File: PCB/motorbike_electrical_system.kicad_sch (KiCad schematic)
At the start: 8 parts, among them U1 L7805, U2 L7805, U3 L7805, U4 ATmega16L-8P

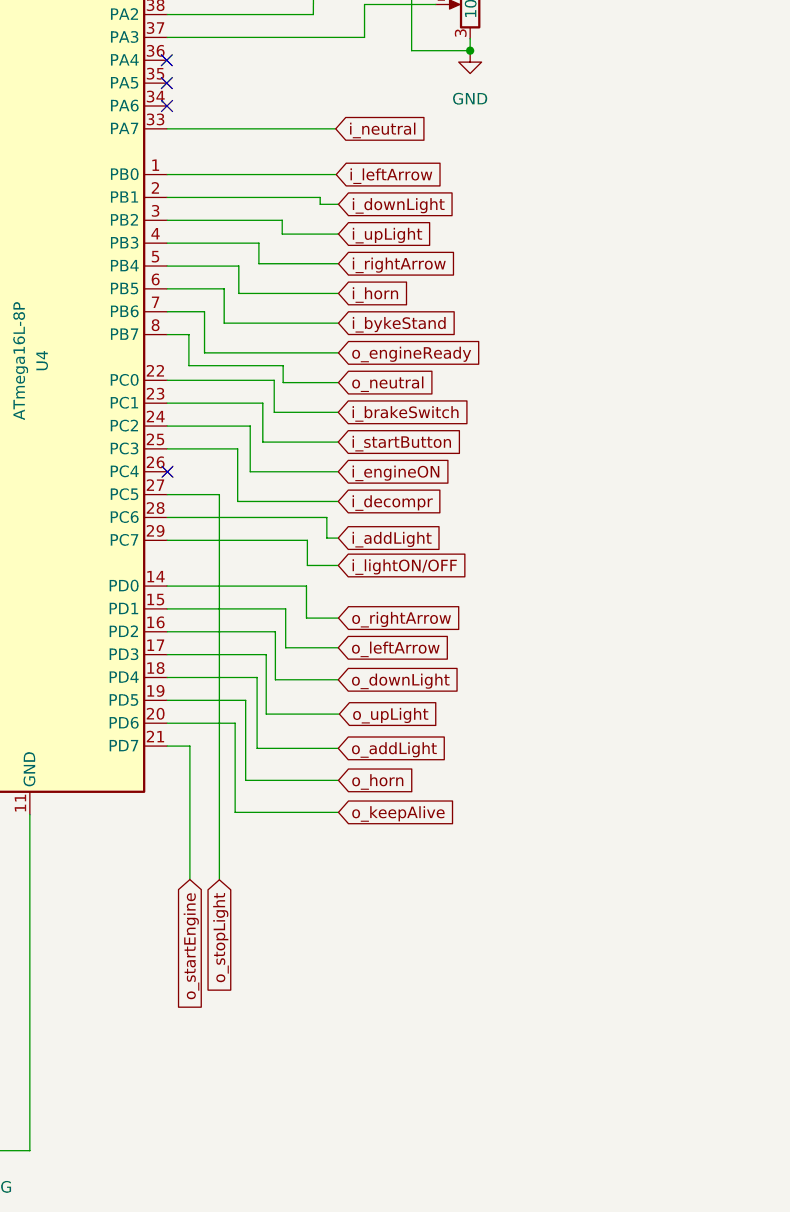
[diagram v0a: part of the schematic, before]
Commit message: feat: power-off button
Because MCU could have a problem for an unpredictable reason, a power-off button has been added to stop the current to the MCU.
But, because I am paranoide and the transistor could have problems, I connected the power-off button yo the MCU too. In this way
it can always shutdown itself
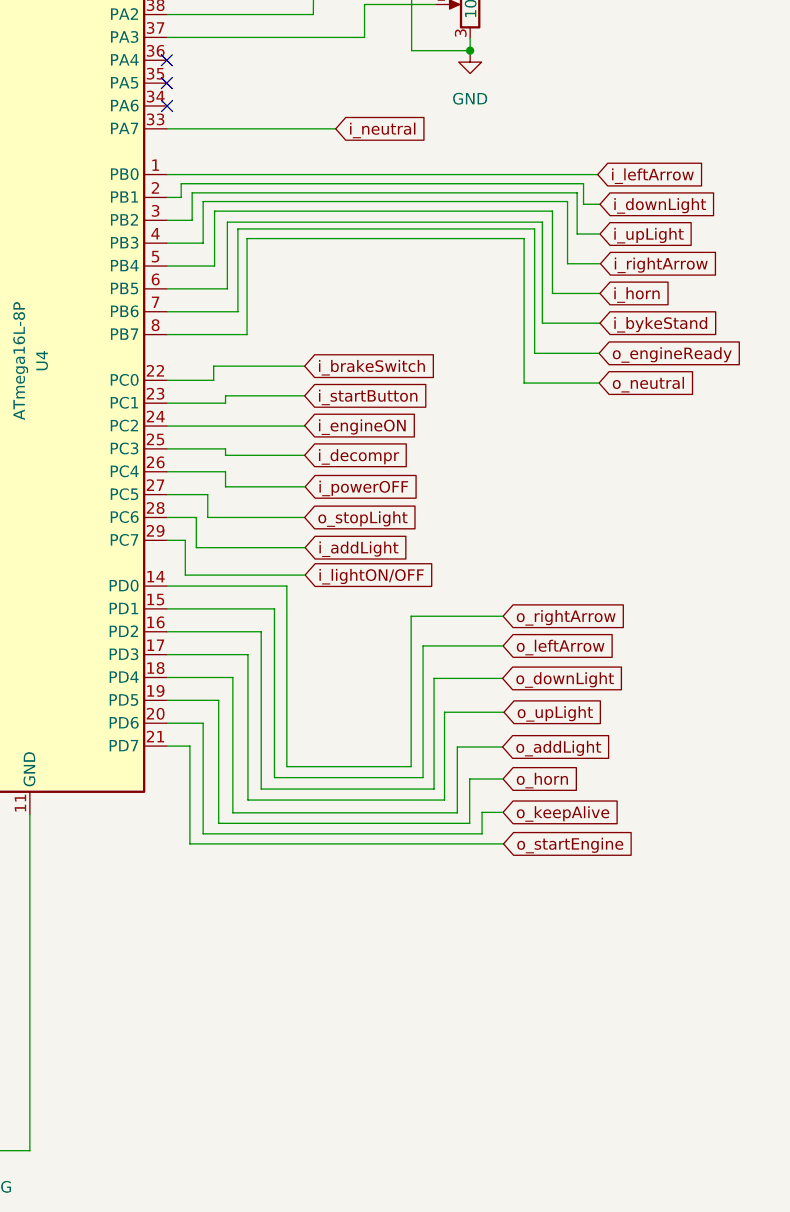
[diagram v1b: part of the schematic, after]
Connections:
- net i_powerOFF: now reaches U4.26 (PC4)
- no-connect marks 9 -> 8

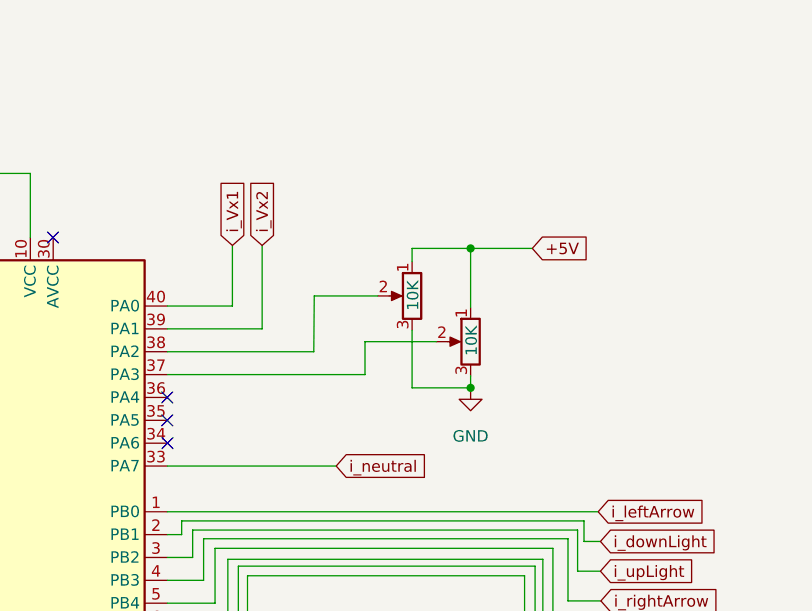
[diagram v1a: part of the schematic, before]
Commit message: Floating BC337 transistors bases fixed, and PowerOFF button management added
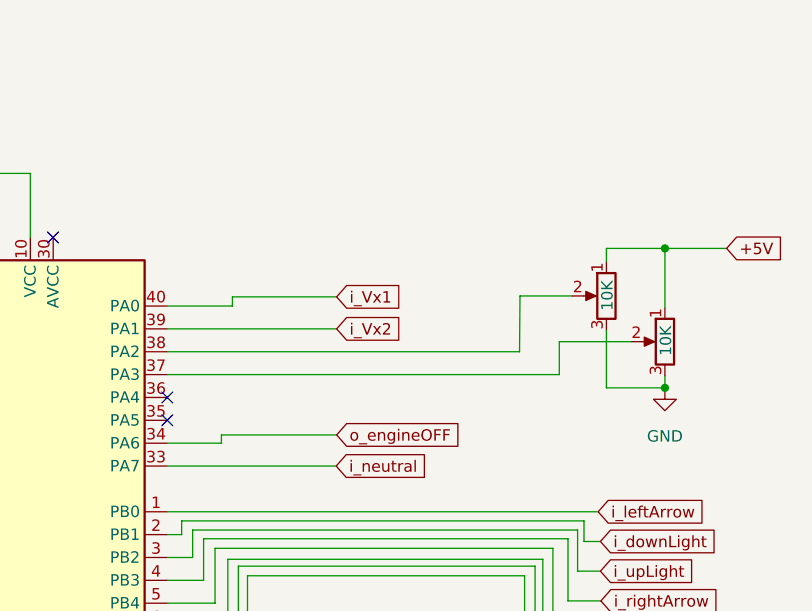
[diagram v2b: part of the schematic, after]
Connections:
- net o_engineOFF: now reaches U4.34 (PA6)
- no-connect marks 8 -> 7

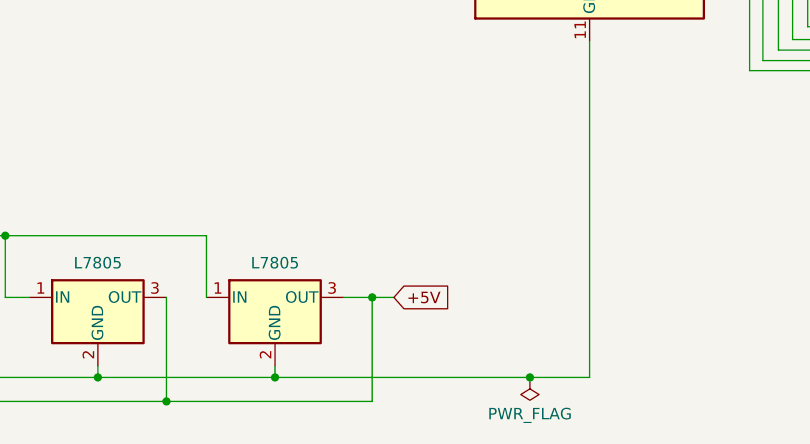
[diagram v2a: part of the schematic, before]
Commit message: - Other floating BC337 transistors bases fixed - USB port missing fixed - Small enhancements
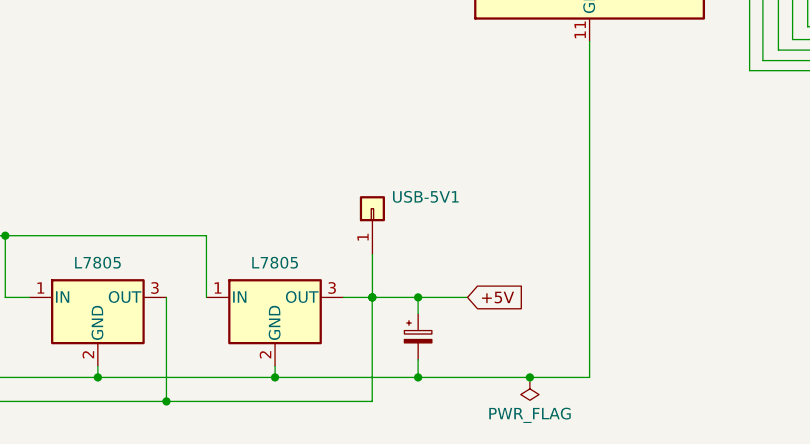
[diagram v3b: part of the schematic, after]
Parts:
- added C1: C_Polarized_Small, Capacitor_THT:CP_Radial_D8.0mm_P2.50mm, symbol Device:C_Polarized_Small
- added USB-5V1: Conn_01x01, Connector_Wire:SolderWire-1.5sqmm_1x01_D1.7mm_OD3.9mm, symbol Connector_Generic:Conn_01x01
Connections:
- net +5V: now also C1.1, USB-5V1.1 (Pin_1)
- net GND: now also C1.2
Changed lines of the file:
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@@
   )
   (bus_alias "port-b" (members "PB0" "PB1" "PB2" "PB3" "PB4" "PB5" "PB6" "PB7"))
+  (junction (at 108.3564 185.42) (diameter 0) (color 0 0 0 0)
+  )
   (junction (at 92.456 185.42) (diameter 0) (color 0 0 0 0)
   )
+  (junction (at 103.2764 176.53) (diameter 0) (color 0 0 0 0)
+  )
   (junction (at 42.291 169.672) (diameter 0) (color 0 0 0 0)
   )
@@
   )
   (junction (at 37.211 185.42) (diameter 0) (color 0 0 0 0)
+  )
+  (junction (at 108.3564 176.53) (diameter 0) (color 0 0 0 0)
   )
   (junction (at 52.451 185.42) (diameter 0) (color 0 0 0 0)
@@
     (stroke (width 0) (type default) (color 0 0 0 0))
   )
+  (wire (pts (xy 103.2764 171.7548) (xy 103.2764 176.53))
+    (stroke (width 0) (type default) (color 0 0 0 0))
+  )
   (wire (pts (xy 149.1488 109.982) (xy 149.1488 111.6584))
     (stroke (width 0) (type default) (color 0 0 0 0))
@@
     (stroke (width 0) (type default) (color 0 0 0 0))
   )
+  (wire (pts (xy 108.3564 176.53) (xy 113.8428 176.53))
+    (stroke (width 0) (type default) (color 0 0 0 0))
+  )
   (wire (pts (xy 197.9168 61.8744) (xy 197.9168 63.1952))
     (stroke (width 0) (type default) (color 0 0 0 0))
@@
     (stroke (width 0) (type default) (color 0 0 0 0))
   )
+  (wire (pts (xy 108.3564 185.42) (xy 120.777 185.42))
+    (stroke (width 0) (type default) (color 0 0 0 0))
+  )
   (wire (pts (xy 142.6464 79.502) (xy 144.2212 79.502))
     (stroke (width 0) (type default) (color 0 0 0 0))
@@
     (stroke (width 0) (type default) (color 0 0 0 0))
   )
+  (wire (pts (xy 108.3564 183.4388) (xy 108.3564 185.42))
+    (stroke (width 0) (type default) (color 0 0 0 0))
+  )
   (wire (pts (xy 142.6464 137.922) (xy 146.6596 137.922))
     (stroke (width 0) (type default) (color 0 0 0 0))
@@
     (stroke (width 0) (type default) (color 0 0 0 0))
   )
-  (wire (pts (xy 92.456 185.42) (xy 120.777 185.42))
+  (wire (pts (xy 92.456 185.42) (xy 108.3564 185.42))
     (stroke (width 0) (type default) (color 0 0 0 0))
   )
@@
     (stroke (width 0) (type default) (color 0 0 0 0))
   )
-  (wire (pts (xy 103.251 176.53) (xy 105.664 176.53))
+  (wire (pts (xy 103.251 176.53) (xy 103.2764 176.53))
     (stroke (width 0) (type default) (color 0 0 0 0))
   )
@@
     (stroke (width 0) (type default) (color 0 0 0 0))
   )
+  (wire (pts (xy 108.3564 176.53) (xy 108.3564 178.3588))
+    (stroke (width 0) (type default) (color 0 0 0 0))
+  )
   (wire (pts (xy 30.988 176.403) (xy 30.988 169.672))
     (stroke (width 0) (type default) (color 0 0 0 0))
@@
   )
   (wire (pts (xy 177.6476 147.828) (xy 179.9844 147.828))
+    (stroke (width 0) (type default) (color 0 0 0 0))
+  )
+  (wire (pts (xy 103.2764 176.53) (xy 108.3564 176.53))
     (stroke (width 0) (type default) (color 0 0 0 0))
   )
@@
     )
   )
-  (global_label "+5V" (shape input) (at 105.664 176.53 0) (fields_autoplaced)
-    (effects (font (size 1.27 1.27)) (justify left))
-    (property "Riferimenti inter-foglio" "${INTERSHEET_REFS}" (id 0) (at 111.9476 176.4506 0)
+  (global_label "+5V" (shape input) (at 113.8428 176.53 0) (fields_autoplaced)
+    (effects (font (size 1.27 1.27)) (justify left))
+    (property "Riferimenti inter-foglio" "${INTERSHEET_REFS}" (id 0) (at 120.1264 176.4506 0)
       (effects (font (size 1.27 1.27)) (justify left) hide)
     )
@@
       (effects (font (size 1.27 1.27)) (justify left) hide)
     )
+  )
+  (symbol (lib_id "Device:C_Polarized_Small") (at 108.3564 180.8988 0) (unit 1)
+    (in_bom yes) (on_board yes) (fields_autoplaced)
+    (property "Reference" "C1" (id 0) (at 105.1814 181.6228 0)
+      (effects (font (size 1.27 1.27)) (justify right) hide)
+    )
+    (property "Value" "C_Polarized_Small" (id 1) (at 105.1814 179.0828 0)
+      (effects (font (size 1.27 1.27)) (justify right) hide)
+    )
+    (property "Footprint" "Capacitor_THT:CP_Radial_D8.0mm_P2.50mm" (id 2) (at 108.3564 180.8988 0)
+      (effects (font (size 1.27 1.27)) hide)
+    )
+    (property "Datasheet" "~" (id 3) (at 108.3564 180.8988 0)
+      (effects (font (size 1.27 1.27)) hide)
+    )
+    (pin "1")
+    (pin "2")
   )
   (symbol (lib_id "Device:C_Polarized_Small") (at 37.211 177.8 0) (unit 1)
@@
     (pin "1")
   )
+  (symbol (lib_id "Connector_Generic:Conn_01x01") (at 103.2764 166.6748 90) (unit 1)
+    (in_bom yes) (on_board yes) (fields_autoplaced)
+    (property "Reference" "USB-5V1" (id 0) (at 105.41 165.4047 90)
+      (effects (font (size 1.27 1.27)) (justify right))
+    )
+    (property "Value" "Conn_01x01" (id 1) (at 105.41 167.9447 90)
+      (effects (font (size 1.27 1.27)) (justify right) hide)
+    )
+    (property "Footprint" "Connector_Wire:SolderWire-1.5sqmm_1x01_D1.7mm_OD3.9mm" (id 2) (at 103.2764 166.6748 0)
+      (effects (font (size 1.27 1.27)) hide)
+    )
+    (property "Datasheet" "~" (id 3) (at 103.2764 166.6748 0)
+      (effects (font (size 1.27 1.27)) hide)
+    )
+    (pin "1")
+  )
   (symbol (lib_id "Device:R_Potentiometer") (at 197.9168 58.0644 0) (mirror y) (unit 1)
     (in_bom yes) (on_board yes)
@@
       (reference "Bike_stand1") (unit 1) (value "Conn_01x02") (footprint "Connector_PinSocket_2.54mm:PinSocket_1x02_P2.54mm_Vertical")
     )
+    (path "/04aa5b9a-f3dc-49cf-8ddb-d1b86befd9ee"
+      (reference "C1") (unit 1) (value "C_Polarized_Small") (footprint "Capacitor_THT:CP_Radial_D8.0mm_P2.50mm")
+    )
     (path "/30dc0a46-b131-4274-a1fd-5018492748b9"
       (reference "C9") (unit 1) (value "C_Polarized_Small") (footprint "Capacitor_THT:CP_Radial_D8.0mm_P2.50mm")
     )
-    (path "/44e17612-9f2f-476d-8e41-268bb036a54a/b28cc80c-4c07-41f6-b6f7-eda42569a9ee"
-      (reference "D1") (unit 1) (value "DIODE") (footprint "Diode_THT:D_DO-34_SOD68_P7.62mm_Horizontal")
-    )
-    (path "/44e17612-9f2f-476d-8e41-268bb036a54a/d5f9a755-b7e5-4665-a302-c881c35b3efb"
-      (reference "D2") (unit 1) (value "DIODE") (footprint "Diode_THT:D_DO-34_SOD68_P7.62mm_Horizontal")
-    )
     (path "/44e17612-9f2f-476d-8e41-268bb036a54a/4741befc-10fc-4c1d-aee4-90bbd7f37f03"
       (reference "D3") (unit 1) (value "2V") (footprint "Diode_THT:D_DO-35_SOD27_P7.62mm_Horizontal")
@@
       (reference "RA41") (unit 1) (value "4K") (footprint "Resistor_THT:R_Axial_DIN0207_L6.3mm_D2.5mm_P7.62mm_Horizontal")
     )
+    (path "/44e17612-9f2f-476d-8e41-268bb036a54a/e071729c-7429-4507-8012-866df5a0c2ef"
+      (reference "RA42") (unit 1) (value "100K") (footprint "Resistor_THT:R_Axial_DIN0207_L6.3mm_D2.5mm_P7.62mm_Horizontal")
+    )
+    (path "/44e17612-9f2f-476d-8e41-268bb036a54a/2c5e0e6a-d3a8-4ba2-bddc-6b7eeb6d722b"
+      (reference "RA43") (unit 1) (value "100K") (footprint "Resistor_THT:R_Axial_DIN0207_L6.3mm_D2.5mm_P7.62mm_Horizontal")
+    )
+    (path "/44e17612-9f2f-476d-8e41-268bb036a54a/cc860c9f-2cd0-4236-b544-8ab5bee0a426"
+      (reference "RA44") (unit 1) (value "100K") (footprint "Resistor_THT:R_Axial_DIN0207_L6.3mm_D2.5mm_P7.62mm_Horizontal")
+    )
     (path "/dfeffa1f-9119-4780-8aed-ab76c9242c17"
       (reference "RV1") (unit 1) (value "10K") (footprint "Potentiometer_THT:Potentiometer_Bourns_3296W_Vertical")
@@
       (reference "U4") (unit 1) (value "ATmega16L-8P") (footprint "Package_DIP:DIP-40_W15.24mm")
     )
+    (path "/7ace0198-87bb-4486-9d09-86f40ed410fe"
+      (reference "USB-5V1") (unit 1) (value "Conn_01x01") (footprint "Connector_Wire:SolderWire-1.5sqmm_1x01_D1.7mm_OD3.9mm")
+    )
     (path "/44e17612-9f2f-476d-8e41-268bb036a54a/652dfdb8-0440-480c-872f-86be3f84a68f"
